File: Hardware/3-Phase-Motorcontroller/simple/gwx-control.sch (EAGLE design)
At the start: 26 parts, among them IC1 74LS02D, IC2 74LS123D, T1 BC850, T2 BC850

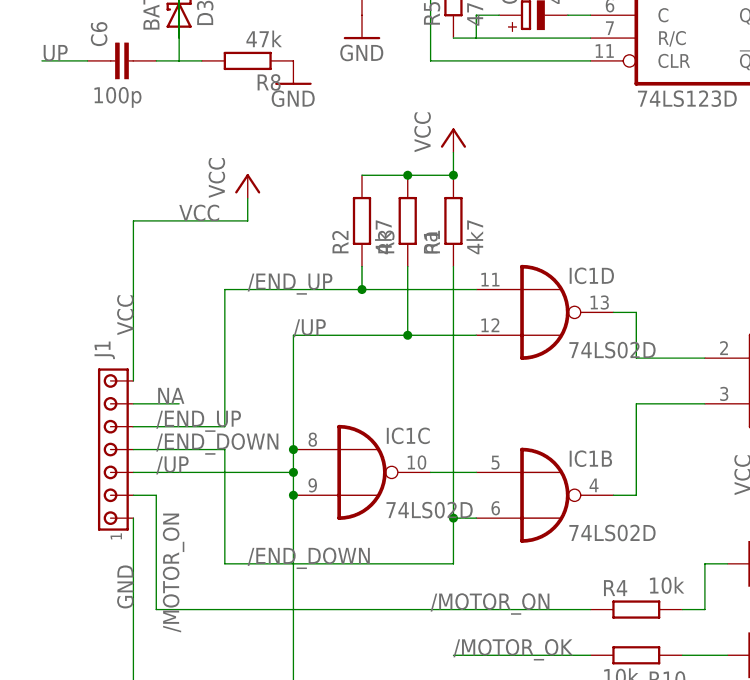
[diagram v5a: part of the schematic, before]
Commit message: LEDs added
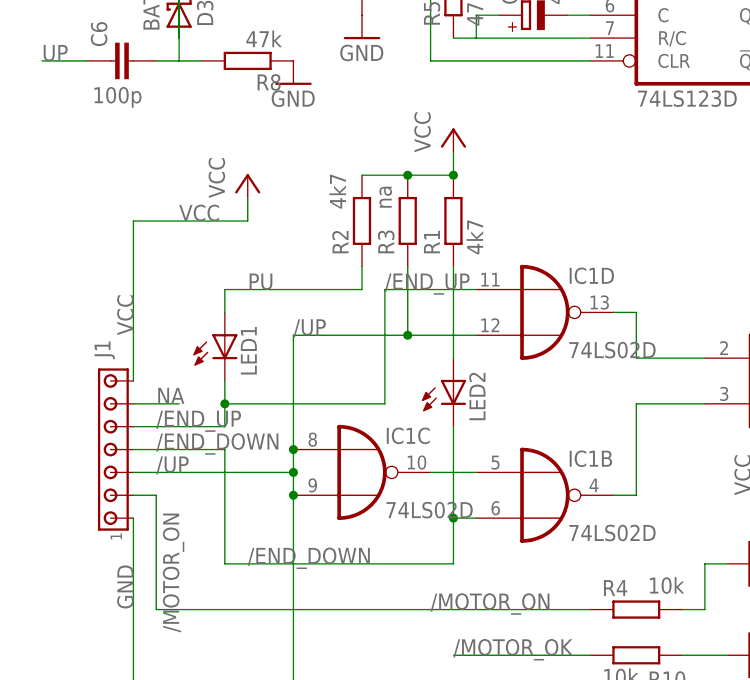
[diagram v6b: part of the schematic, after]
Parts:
- added LED1, LED2: (no value), eagle-ltspice:LED_ESML0603
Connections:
- new net N$15: LED2.A, R1.1
- new net PU: LED1.A, R2.1
- net /END_DOWN: now also LED2.C; no longer R1.1
- net /END_UP: now also LED1.C; no longer R2.1
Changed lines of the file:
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@@
 <part name="R10" library="resistor" deviceset="R-EU_" device="R0603" value="10k"/>
 <part name="D2" library="diode" deviceset="BAT54C" device=""/>
+<part name="LED1" library="eagle-ltspice" deviceset="LED_E" device="SML0603"/>
+<part name="LED2" library="eagle-ltspice" deviceset="LED_E" device="SML0603"/>
 </parts>
 <sheets>
@@
 <attribute name="VALUE" x="35.56" y="28.1686" size="1.778" layer="96"/>
 </instance>
-<instance part="R1" gate="G$1" x="25.4" y="83.82" rot="R90"/>
-<instance part="R2" gate="G$1" x="15.24" y="83.82" rot="R90"/>
-<instance part="R3" gate="G$1" x="20.32" y="83.82" rot="R90"/>
+<instance part="R1" gate="G$1" x="25.4" y="83.82" smashed="yes" rot="R90">
+<attribute name="NAME" x="23.9014" y="80.01" size="1.778" layer="95" rot="R90"/>
+<attribute name="VALUE" x="28.702" y="80.01" size="1.778" layer="96" rot="R90"/>
+</instance>
+<instance part="R2" gate="G$1" x="15.24" y="83.82" smashed="yes" rot="R90">
+<attribute name="NAME" x="13.7414" y="80.01" size="1.778" layer="95" rot="R90"/>
+<attribute name="VALUE" x="13.462" y="85.09" size="1.778" layer="96" rot="R90"/>
+</instance>
+<instance part="R3" gate="G$1" x="20.32" y="83.82" smashed="yes" rot="R90">
+<attribute name="NAME" x="18.8214" y="80.01" size="1.778" layer="95" rot="R90"/>
+<attribute name="VALUE" x="18.542" y="85.09" size="1.778" layer="96" rot="R90"/>
+</instance>
 <instance part="P+4" gate="VCC" x="25.4" y="93.98"/>
 <instance part="R4" gate="G$1" x="45.72" y="40.64" smashed="yes">
@@
 </instance>
 <instance part="D2" gate="G$1" x="60.96" y="25.4"/>
+<instance part="LED1" gate="G$1" x="0" y="71.12"/>
+<instance part="LED2" gate="G$1" x="25.4" y="66.04"/>
 </instances>
 <busses>
@@
 <net name="/END_UP" class="0">
 <segment>
-<pinref part="IC1" gate="D" pin="I0"/>
-<wire x1="27.94" y1="76.2" x2="15.24" y2="76.2" width="0.1524" layer="91"/>
-<label x="2.54" y="76.2" size="1.778" layer="95"/>
-<wire x1="15.24" y1="76.2" x2="0" y2="76.2" width="0.1524" layer="91"/>
-<wire x1="0" y1="76.2" x2="0" y2="60.96" width="0.1524" layer="91"/>
 <pinref part="J1" gate="G$1" pin="5"/>
 <wire x1="-10.16" y1="60.96" x2="0" y2="60.96" width="0.1524" layer="91"/>
 <label x="-7.62" y="60.96" size="1.778" layer="95"/>
-<pinref part="R2" gate="G$1" pin="1"/>
-<wire x1="15.24" y1="78.74" x2="15.24" y2="76.2" width="0.1524" layer="91"/>
-<junction x="15.24" y="76.2"/>
+<pinref part="LED1" gate="G$1" pin="C"/>
+<wire x1="0" y1="66.04" x2="0" y2="63.5" width="0.1524" layer="91"/>
+<pinref part="IC1" gate="D" pin="I0"/>
+<wire x1="0" y1="63.5" x2="0" y2="60.96" width="0.1524" layer="91"/>
+<wire x1="27.94" y1="76.2" x2="17.78" y2="76.2" width="0.1524" layer="91"/>
+<wire x1="17.78" y1="76.2" x2="17.78" y2="63.5" width="0.1524" layer="91"/>
+<wire x1="17.78" y1="63.5" x2="0" y2="63.5" width="0.1524" layer="91"/>
+<junction x="0" y="63.5"/>
+<label x="17.78" y="76.2" size="1.778" layer="95"/>
 </segment>
 </net>
@@
 <wire x1="-10.16" y1="58.42" x2="0" y2="58.42" width="0.1524" layer="91"/>
 <wire x1="0" y1="58.42" x2="0" y2="45.72" width="0.1524" layer="91"/>
-<pinref part="R1" gate="G$1" pin="1"/>
-<wire x1="25.4" y1="78.74" x2="25.4" y2="50.8" width="0.1524" layer="91"/>
+<pinref part="LED2" gate="G$1" pin="C"/>
+<wire x1="25.4" y1="60.96" x2="25.4" y2="50.8" width="0.1524" layer="91"/>
 <junction x="25.4" y="50.8"/>
 </segment>
@@
 </segment>
 </net>
+<net name="N$15" class="0">
+<segment>
+<pinref part="LED2" gate="G$1" pin="A"/>
+<pinref part="R1" gate="G$1" pin="1"/>
+<wire x1="25.4" y1="68.58" x2="25.4" y2="78.74" width="0.1524" layer="91"/>
+</segment>
+</net>
+<net name="PU" class="0">
+<segment>
+<label x="2.54" y="76.2" size="1.778" layer="95"/>
+<wire x1="15.24" y1="76.2" x2="0" y2="76.2" width="0.1524" layer="91"/>
+<pinref part="R2" gate="G$1" pin="1"/>
+<wire x1="15.24" y1="78.74" x2="15.24" y2="76.2" width="0.1524" layer="91"/>
+<pinref part="LED1" gate="G$1" pin="A"/>
+<wire x1="0" y1="73.66" x2="0" y2="76.2" width="0.1524" layer="91"/>
+</segment>
+</net>
